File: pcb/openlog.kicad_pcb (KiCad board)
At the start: 2 copper layers, 36 x 36 mm, 25 parts

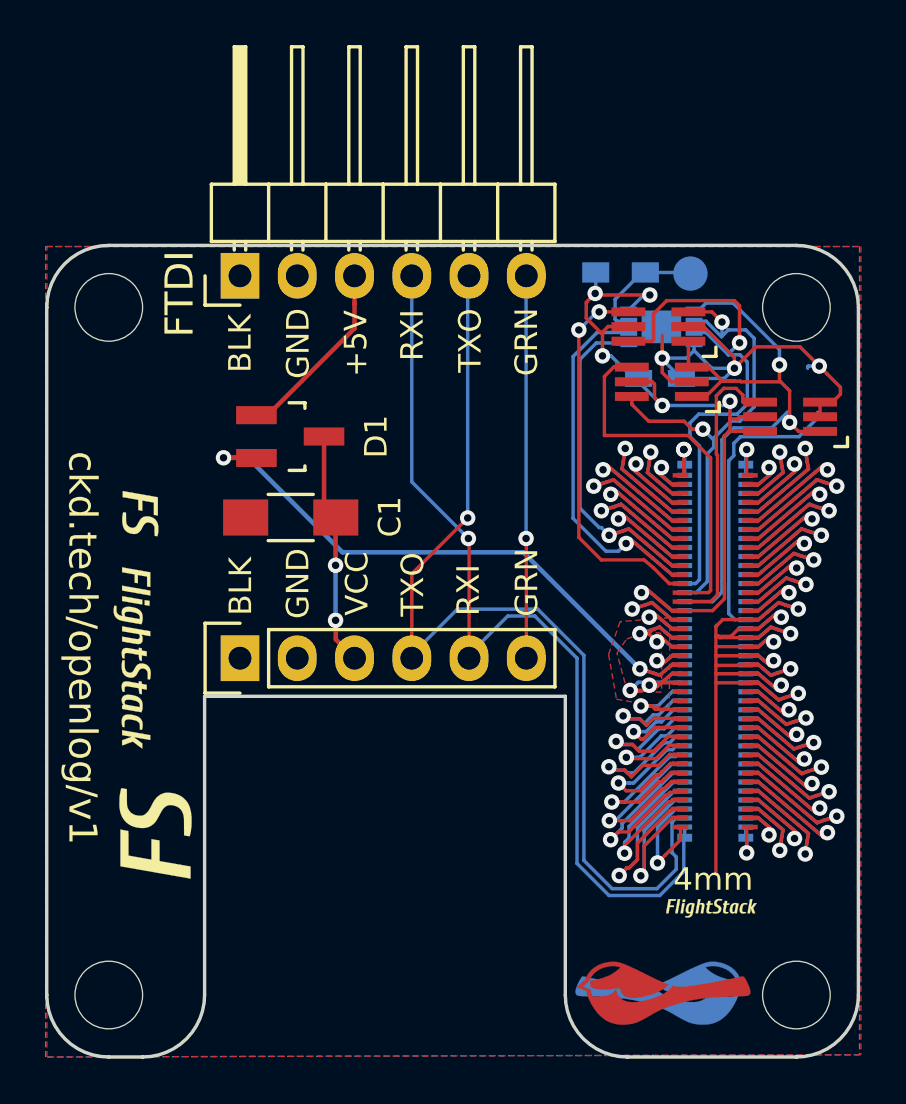
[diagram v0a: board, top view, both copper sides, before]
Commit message: Add license information to many files. PCB design files are CC-BY and code is MIT license.
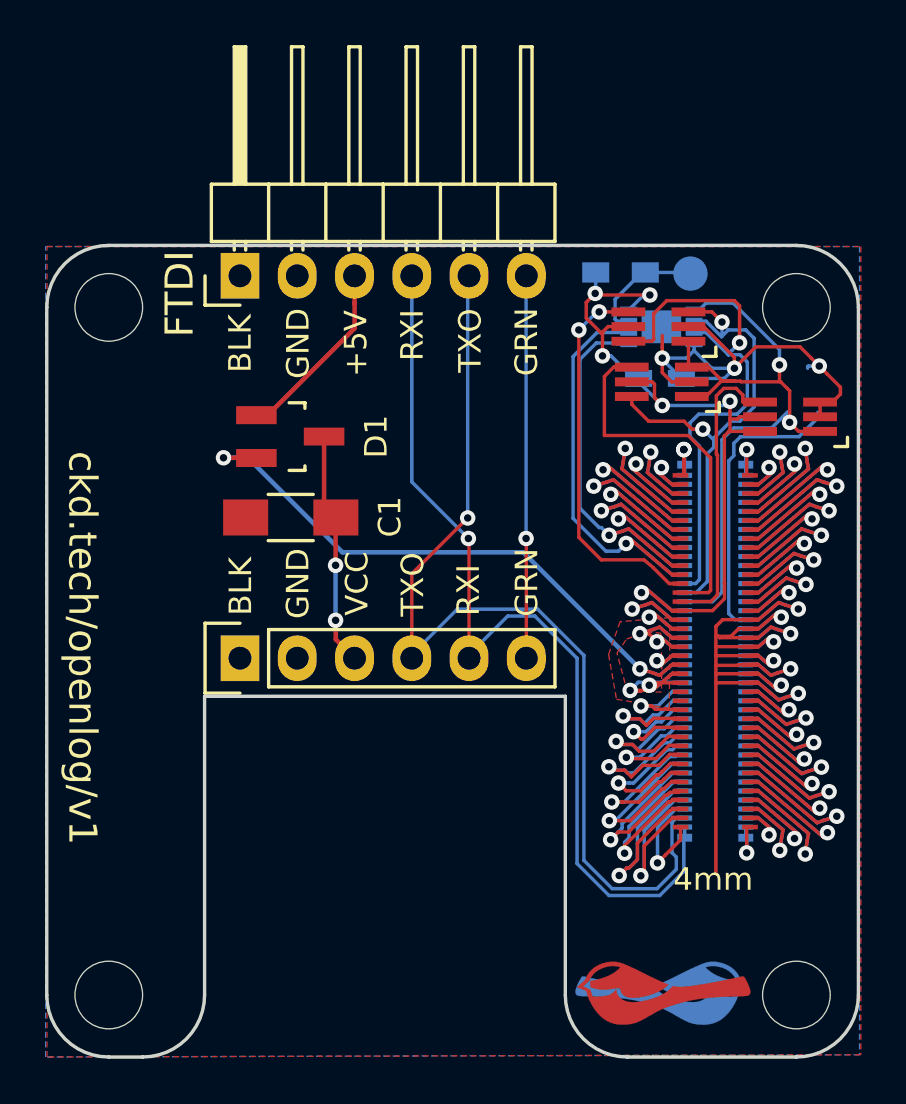
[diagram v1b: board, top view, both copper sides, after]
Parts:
- removed the G*** at (133.8, 108.3) (x2)
- removed the G*** at (159.6, 119.4)
- removed the G*** at (159.5, 119.4)
- removed the G*** at (134.8, 116.1)
- removed the G*** at (134.2, 101.9)
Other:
- board text added: "Copyright 2016 Chickadee Tech LLC, <add attributions here> This work is licensed under the Creative Commons Attribution 4.0 International License. To view a copy of this license, visit http://creativecommons.org/licenses/by/4.0/ or send a letter to Creative Commons, PO Box 1866, Mountain View, CA 94042, USA."
- board text added: "Remove all Chickadee Tech trademarks before making your own board. The Chickadee logo and Polystack logo are owned by Chickadee Tech. You may license the Polystack logo for free by emailing support@chickadee.tech and receiving express written permission from Chickadee Tech LLC."
